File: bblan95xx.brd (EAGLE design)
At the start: 50 x 50 mm, 52 parts, among them IC1 LAN9512, IC2 93ST, Q1 25MHz

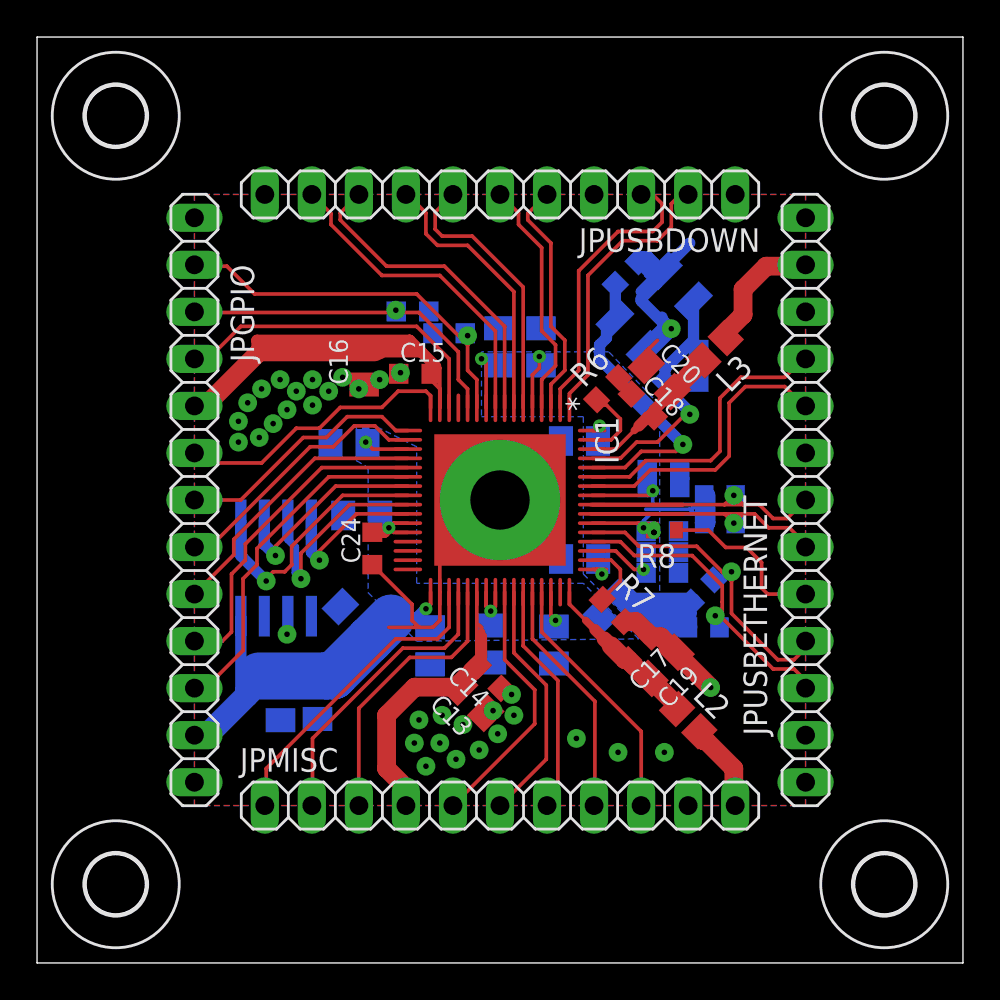
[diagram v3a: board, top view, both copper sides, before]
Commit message: add more vias to connect GND planes
Signed-off-by: Stephan Baerwolf <stephan@matrixstorm.com>
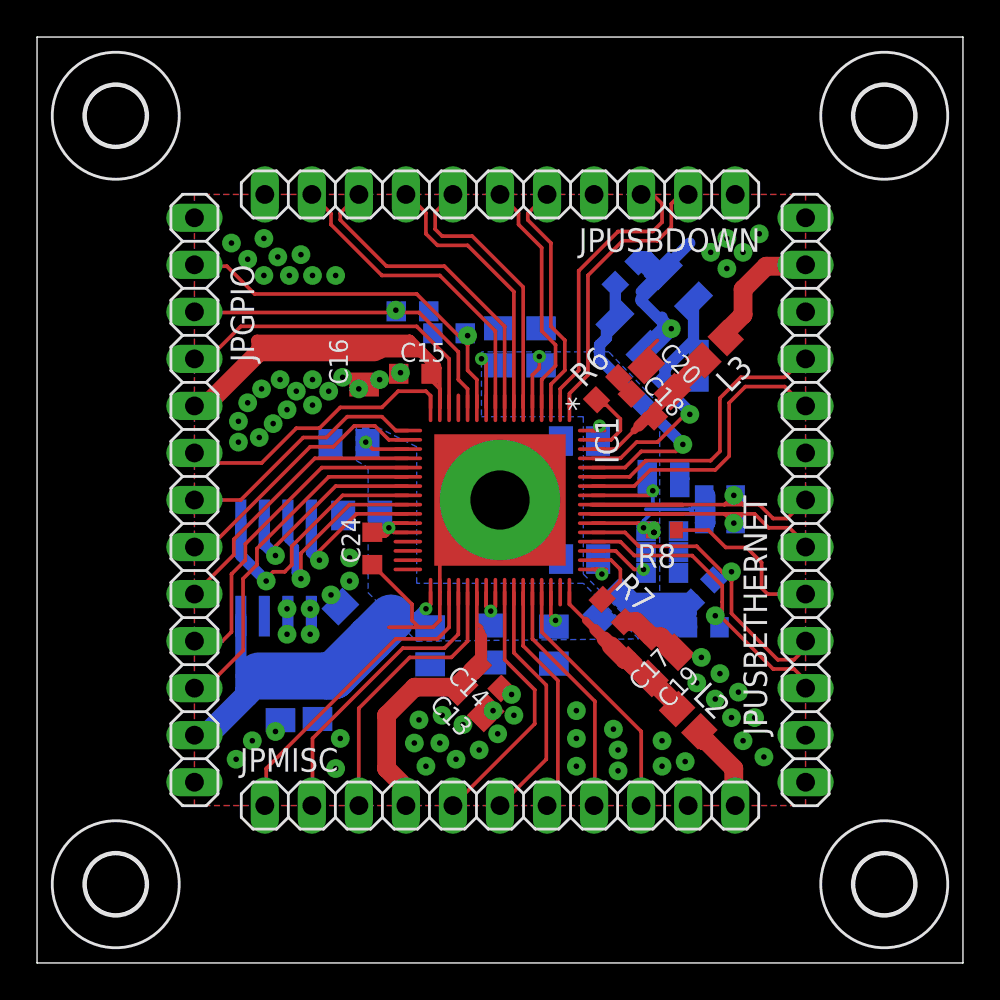
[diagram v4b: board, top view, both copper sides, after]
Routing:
- net GND: track 37.0 -> 34.3 mm, vias 35 -> 74
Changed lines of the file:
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@@
 <wire x1="33.680078125" y1="17.60913125" x2="34.50888125" y2="16.780328125" width="1.016" layer="1"/>
 <wire x1="34.50888125" y1="16.780328125" x2="34.50888125" y2="16.74111875" width="1.016" layer="1"/>
-<wire x1="34.50888125" y1="16.74111875" x2="36.375" y2="14.875" width="1.016" layer="1"/>
-<via x="36.375" y="14.875" extent="1-16" drill="0.3" diameter="1.016" shape="octagon"/>
-<via x="33.875" y="11.375" extent="1-16" drill="0.3" diameter="1.016" shape="octagon"/>
-<via x="31.375" y="11.375" extent="1-16" drill="0.3" diameter="1.016" shape="octagon"/>
+<via x="35.625" y="15.125" extent="1-16" drill="0.3" diameter="1.016" shape="octagon"/>
+<via x="33.75" y="10.625" extent="1-16" drill="0.3" diameter="1.016" shape="octagon"/>
+<via x="31.375" y="11.5" extent="1-16" drill="0.3" diameter="1.016" shape="octagon"/>
 <via x="29.125" y="12.125" extent="1-16" drill="0.3" diameter="1.016" shape="octagon"/>
 <wire x1="21.75" y1="20.023" x2="21.75" y2="18.5" width="0.2" layer="1"/>
@@
 <contactref element="C29" pad="1"/>
 <contactref element="C30" pad="1"/>
+<via x="29.125" y="13.625" extent="1-16" drill="0.3" diameter="1.016" shape="octagon"/>
+<via x="29.125" y="10.625" extent="1-16" drill="0.3" diameter="1.016" shape="octagon"/>
+<via x="31.125" y="12.625" extent="1-16" drill="0.3" diameter="1.016" shape="octagon"/>
+<via x="31.375" y="10.375" extent="1-16" drill="0.3" diameter="1.016" shape="octagon"/>
+<via x="16.375" y="12.125" extent="1-16" drill="0.3" diameter="1.016" shape="octagon"/>
+<via x="16.125" y="10.5" extent="1-16" drill="0.3" diameter="1.016" shape="octagon"/>
+<via x="33.75" y="12" extent="1-16" drill="0.3" diameter="1.016" shape="octagon"/>
+<via x="35" y="10.875" extent="1-16" drill="0.3" diameter="1.016" shape="octagon"/>
+<via x="11.625" y="12" extent="1-16" drill="0.3" diameter="1.016" shape="octagon"/>
+<via x="10.75" y="11" extent="1-16" drill="0.3" diameter="1.016" shape="octagon"/>
+<via x="12.875" y="12.5" extent="1-16" drill="0.3" diameter="1.016" shape="octagon"/>
+<via x="14.75" y="17.75" extent="1-16" drill="0.3" diameter="1.016" shape="octagon"/>
+<via x="15.875" y="19.875" extent="1-16" drill="0.3" diameter="1.016" shape="octagon"/>
+<via x="16.875" y="21.875" extent="1-16" drill="0.3" diameter="1.016" shape="octagon"/>
+<via x="16.875" y="20.625" extent="1-16" drill="0.3" diameter="1.016" shape="octagon"/>
+<via x="13.5" y="19.125" extent="1-16" drill="0.3" diameter="1.016" shape="octagon"/>
+<via x="14.75" y="19.125" extent="1-16" drill="0.3" diameter="1.016" shape="octagon"/>
+<via x="16.125" y="37.125" extent="1-16" drill="0.3" diameter="1.016" shape="octagon"/>
+<via x="14.875" y="37.125" extent="1-16" drill="0.3" diameter="1.016" shape="octagon"/>
+<via x="13.625" y="37.125" extent="1-16" drill="0.3" diameter="1.016" shape="octagon"/>
+<via x="12.25" y="37.125" extent="1-16" drill="0.3" diameter="1.016" shape="octagon"/>
+<via x="11.375" y="38" extent="1-16" drill="0.3" diameter="1.016" shape="octagon"/>
+<via x="10.5" y="38.875" extent="1-16" drill="0.3" diameter="1.016" shape="octagon"/>
+<via x="13" y="38.125" extent="1-16" drill="0.3" diameter="1.016" shape="octagon"/>
+<via x="12.25" y="39.125" extent="1-16" drill="0.3" diameter="1.016" shape="octagon"/>
+<via x="14.25" y="38.25" extent="1-16" drill="0.3" diameter="1.016" shape="octagon"/>
+<via x="36.375" y="38.375" extent="1-16" drill="0.3" diameter="1.016" shape="octagon"/>
+<via x="37.25" y="37.5" extent="1-16" drill="0.3" diameter="1.016" shape="octagon"/>
+<via x="37.25" y="39.125" extent="1-16" drill="0.3" diameter="1.016" shape="octagon"/>
+<via x="38.125" y="38.375" extent="1-16" drill="0.3" diameter="1.016" shape="octagon"/>
+<via x="39" y="39.375" extent="1-16" drill="0.3" diameter="1.016" shape="octagon"/>
+<via x="35.875" y="16.5" extent="1-16" drill="0.3" diameter="1.016" shape="octagon"/>
+<via x="36.875" y="15.625" extent="1-16" drill="0.3" diameter="1.016" shape="octagon"/>
+<via x="36.625" y="14.25" extent="1-16" drill="0.3" diameter="1.016" shape="octagon"/>
+<via x="37.875" y="14.625" extent="1-16" drill="0.3" diameter="1.016" shape="octagon"/>
+<via x="37.5" y="13.25" extent="1-16" drill="0.3" diameter="1.016" shape="octagon"/>
+<via x="38.75" y="13.25" extent="1-16" drill="0.3" diameter="1.016" shape="octagon"/>
+<via x="38.125" y="12" extent="1-16" drill="0.3" diameter="1.016" shape="octagon"/>
+<via x="39.25" y="11.125" extent="1-16" drill="0.3" diameter="1.016" shape="octagon"/>
 </signal>
 <signal name="VDD18CORE">

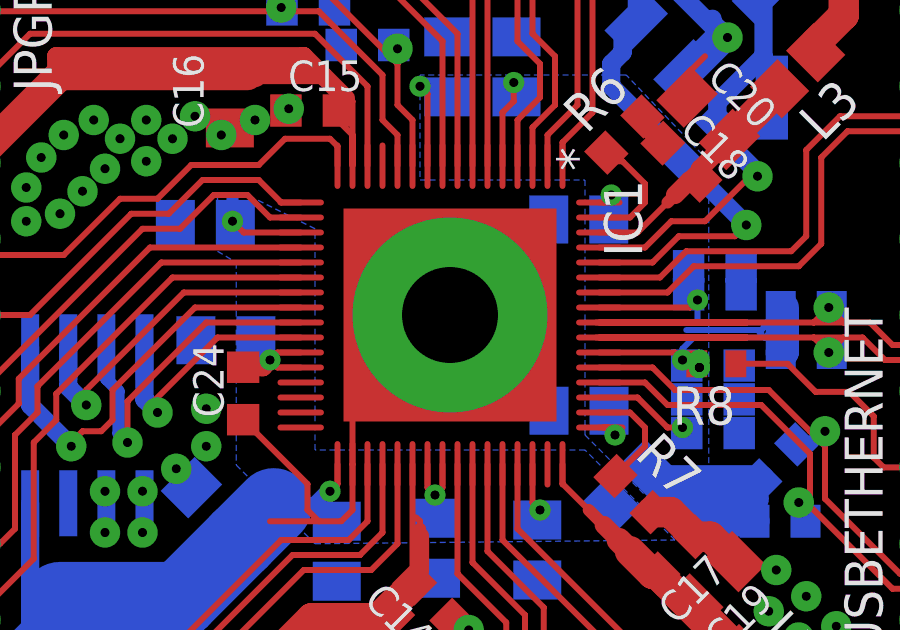
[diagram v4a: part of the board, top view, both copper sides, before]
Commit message: add also thermal vias to main IC
Signed-off-by: Stephan Baerwolf <stephan@matrixstorm.com>
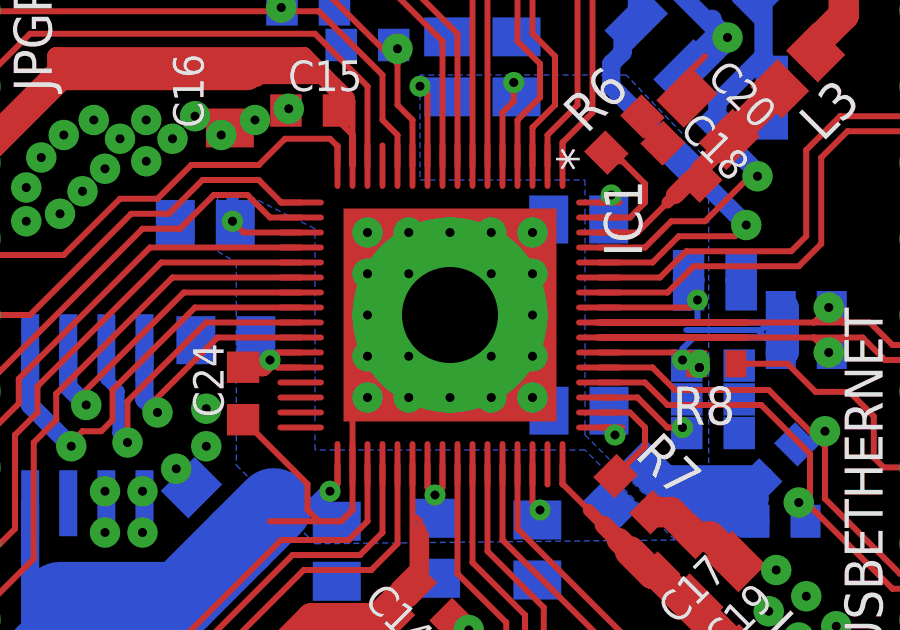
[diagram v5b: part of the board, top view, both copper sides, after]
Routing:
- net GND: vias 74 -> 94
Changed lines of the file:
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@@
 <via x="38.125" y="12" extent="1-16" drill="0.3" diameter="1.016" shape="octagon"/>
 <via x="39.25" y="11.125" extent="1-16" drill="0.3" diameter="1.016" shape="octagon"/>
+<via x="22.25" y="27.75" extent="1-16" drill="0.3" diameter="1.016" shape="octagon"/>
+<via x="23.625" y="27.75" extent="1-16" drill="0.3" diameter="1.016" shape="octagon"/>
+<via x="25" y="27.75" extent="1-16" drill="0.3" diameter="1.016" shape="octagon"/>
+<via x="26.375" y="27.75" extent="1-16" drill="0.3" diameter="1.016" shape="octagon"/>
+<via x="27.75" y="27.75" extent="1-16" drill="0.3" diameter="1.016" shape="octagon"/>
+<via x="22.25" y="26.375" extent="1-16" drill="0.3" diameter="1.016" shape="octagon"/>
+<via x="23.625" y="26.375" extent="1-16" drill="0.3" diameter="1.016" shape="octagon"/>
+<via x="26.375" y="26.375" extent="1-16" drill="0.3" diameter="1.016" shape="octagon"/>
+<via x="27.75" y="26.375" extent="1-16" drill="0.3" diameter="1.016" shape="octagon"/>
+<via x="22.25" y="25" extent="1-16" drill="0.3" diameter="1.016" shape="octagon"/>
+<via x="22.25" y="23.625" extent="1-16" drill="0.3" diameter="1.016" shape="octagon"/>
+<via x="22.25" y="22.25" extent="1-16" drill="0.3" diameter="1.016" shape="octagon"/>
+<via x="27.75" y="25" extent="1-16" drill="0.3" diameter="1.016" shape="octagon"/>
+<via x="23.625" y="23.625" extent="1-16" drill="0.3" diameter="1.016" shape="octagon"/>
+<via x="26.375" y="23.625" extent="1-16" drill="0.3" diameter="1.016" shape="octagon"/>
+<via x="27.75" y="23.625" extent="1-16" drill="0.3" diameter="1.016" shape="octagon"/>
+<via x="23.625" y="22.25" extent="1-16" drill="0.3" diameter="1.016" shape="octagon"/>
+<via x="25" y="22.25" extent="1-16" drill="0.3" diameter="1.016" shape="octagon"/>
+<via x="26.375" y="22.25" extent="1-16" drill="0.3" diameter="1.016" shape="octagon"/>
+<via x="27.75" y="22.25" extent="1-16" drill="0.3" diameter="1.016" shape="octagon"/>
 </signal>
 <signal name="VDD18CORE">
